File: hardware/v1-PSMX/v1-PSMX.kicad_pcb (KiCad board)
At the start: 2 copper layers, 3 parts, among them IC1 MAX98357AETE+T, U1 ESP32-S3-WROOM-1

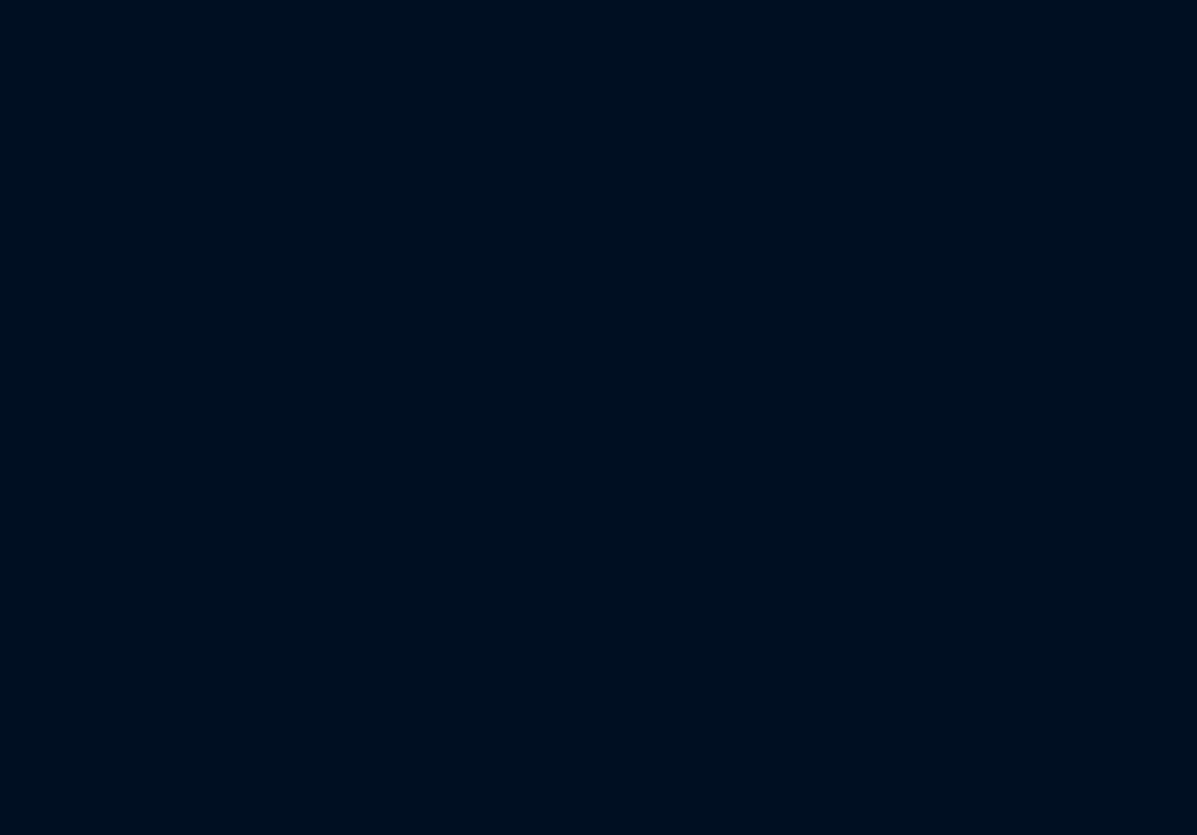
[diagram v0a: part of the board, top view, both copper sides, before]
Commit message: Completed Init work on schematic
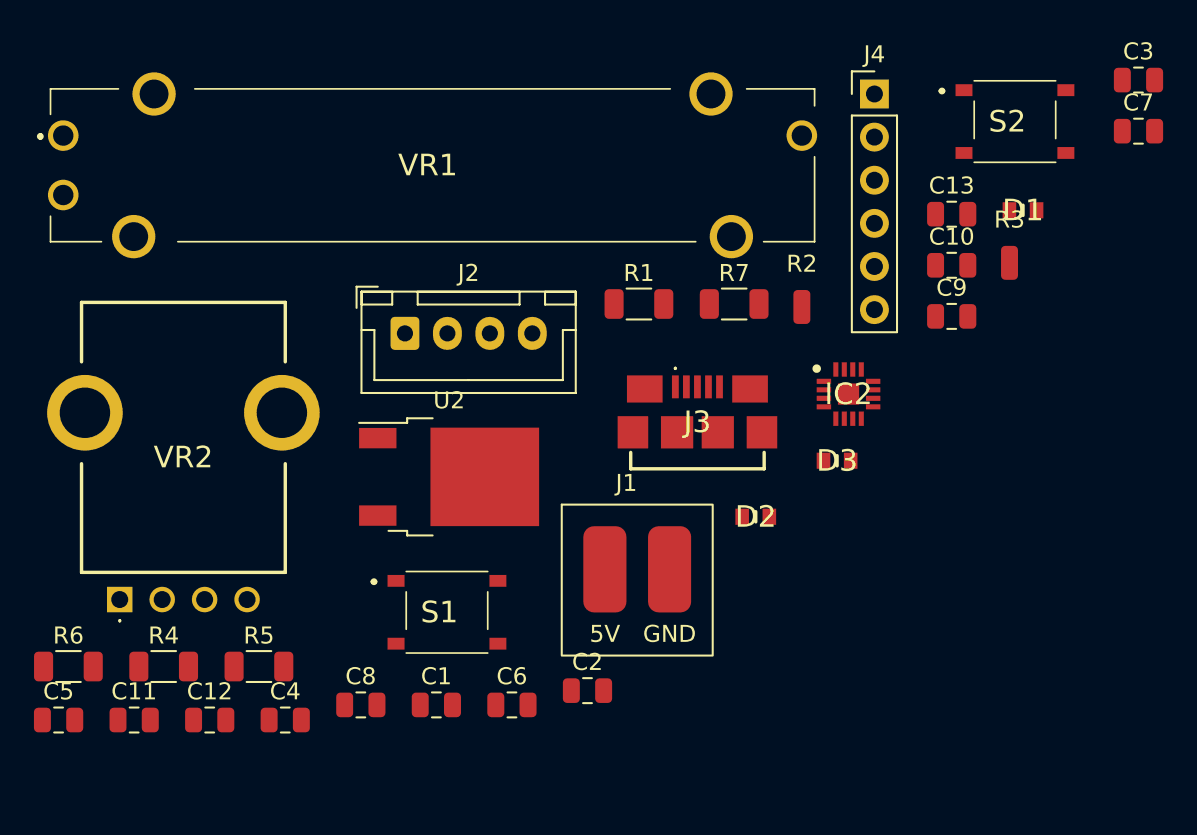
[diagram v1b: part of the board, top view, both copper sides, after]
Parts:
- added C1: 10uF, Capacitor_SMD:C_0805_2012Metric, F.Cu at (126.4, 81.9)
- added C10: 10uF, Capacitor_SMD:C_0805_2012Metric, F.Cu at (156.7, 56.0)
- added C11: 0.1uF, Capacitor_SMD:C_0805_2012Metric, F.Cu at (108.6, 82.8)
- added C12: 0.1uF, Capacitor_SMD:C_0805_2012Metric, F.Cu at (113.0, 82.8)
- added C13: 10uF, Capacitor_SMD:C_0805_2012Metric, F.Cu at (156.7, 53.0)
- added C2: 0.1uF, Capacitor_SMD:C_0805_2012Metric, F.Cu at (135.3, 81.1)
- added C3: 0.1uF, Capacitor_SMD:C_0805_2012Metric, F.Cu at (167.7, 45.1)
- added C4: 10uF, Capacitor_SMD:C_0805_2012Metric, F.Cu at (117.5, 82.8)
- added C5: 10uF, Capacitor_SMD:C_0805_2012Metric, F.Cu at (104.1, 82.8)
- added C6: 10uF, Capacitor_SMD:C_0805_2012Metric, F.Cu at (130.8, 81.9)
- added C7: 0.1uF, Capacitor_SMD:C_0805_2012Metric, F.Cu at (167.7, 48.1)
- added C8: 0.1uF, Capacitor_SMD:C_0805_2012Metric, F.Cu at (121.9, 81.9)
- added C9: 0.1uF, Capacitor_SMD:C_0805_2012Metric, F.Cu at (156.7, 59.0)
- added D1: GG060305100N2P, my-footprints:DIONC1608X70N, F.Cu at (160.9, 52.8)
- added D2: GG060305100N2P, my-footprints:DIONC1608X70N, F.Cu at (145.2, 70.8)
- added D3: GG060305100N2P, my-footprints:DIONC1608X70N, F.Cu at (150.0, 67.5)
- added IC2: MAX98357AETE+T (R), MAX98357AETE+T:QFN50P300X300X80-17N, F.Cu at (150.6, 63.6)
- added J1: +5v_POWER, my-footprints:CUSTOM_5V_SOLDER_PADS, F.Cu at (137.6, 73.9)
- added J2: Conn_01x04, Connector_JST:JST_XH_B4B-XH-A_1x04_P2.50mm_Vertical, F.Cu at (124.5, 60.0)
- added J3: 10118192-0002LF, my-footprints:101181920002LF, F.Cu at (141.7, 65.5)
- added J4: Serial_Breakout, Connector_PinHeader_2.54mm:PinHeader_1x06_P2.54mm_Vertical, F.Cu at (152.2, 45.9)
- added R1: 270ohm, Resistor_SMD:R_1206_3216Metric, F.Cu at (138.3, 58.3)
- added R2: GAIN SELECT, Connector_Wire:SolderWirePad_1x01_SMD_1x2mm, F.Cu at (147.9, 58.5)
- added R3: GAIN SELECT, Connector_Wire:SolderWirePad_1x01_SMD_1x2mm, F.Cu at (160.1, 55.9)
- added R4: 270ohm, Resistor_SMD:R_1206_3216Metric, F.Cu at (110.3, 79.7)
- added R5: 270ohm, Resistor_SMD:R_1206_3216Metric, F.Cu at (115.9, 79.7)
- added R6: 10k_ohm, Resistor_SMD:R_1206_3216Metric, F.Cu at (104.7, 79.7)
- added R7: 220k_ohm, Resistor_SMD:R_1206_3216Metric, F.Cu at (143.9, 58.3)
- added S1: PTS526_SM08_SMTR2_LFS, my-footprints:PTS526SM08SMTR2LFS, F.Cu at (127.0, 76.5)
- added S2: PTS526_SM08_SMTR2_LFS, my-footprints:PTS526SM08SMTR2LFS, F.Cu at (160.4, 47.6)
- added U2: AZ1084-3.3, Package_TO_SOT_SMD:TO-252-2, F.Cu at (127.1, 68.5)
- added VR1: PTA3043-2015DPB104, my-footprints:PTA30432015DPB104, F.Cu at (104.4, 48.4)
- added VR2: P110KH1-0F15BR10K, my-footprints:P110KH10F15BR10K, F.Cu at (107.7, 75.7)
- IC1: value MAX98357AETE+T -> MAX98357AETE+T (L)
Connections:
- IC1 pad 1: unconnected-(IC1-Pad1) -> /DIN_GPIO12
- IC1 pad 10: unconnected-(IC1-Pad10) -> /LEFT_SPK+
- IC1 pad 11: unconnected-(IC1-Pad11) -> GND
- IC1 pad 14: unconnected-(IC1-Pad14) -> /LRCLK_GPIO14
- IC1 pad 15: unconnected-(IC1-Pad15) -> GND
- IC1 pad 16: unconnected-(IC1-Pad16) -> /BCLK_GPIO13
- IC1 pad 17: unconnected-(IC1-Pad17) -> GND
- IC1 pad 2: unconnected-(IC1-Pad2) -> /GAIN_SLOT
- IC1 pad 3: unconnected-(IC1-Pad3) -> GND
- IC1 pad 4: unconnected-(IC1-Pad4) -> /SD_MODE_GPIO11
- IC1 pad 7: unconnected-(IC1-Pad7) -> +5V
- IC1 pad 8: unconnected-(IC1-Pad8) -> +5V
- IC1 pad 9: unconnected-(IC1-Pad9) -> /LEFT_SPK-
- LED1 pad 1: unconnected-(LED1-Pad1) -> +3.3V
- LED1 pad 2: unconnected-(LED1-Pad2) -> Net-(LED1-Pad2)
- LED1 pad 3: unconnected-(LED1-Pad3) -> Net-(LED1-Pad3)
- LED1 pad 4: unconnected-(LED1-Pad4) -> Net-(LED1-Pad4)
- U1 pad 1: Net-(U1-Pad1) -> GND
- U1 pad 13: unconnected-(U1-Pad13) -> /GPIO19_USB_D-
- U1 pad 14: unconnected-(U1-Pad14) -> /GPIO20_USB_D+
- U1 pad 17: unconnected-(U1-Pad17) -> /S_POT_GPIO9
- U1 pad 18: unconnected-(U1-Pad18) -> /V_POT_GPIO10
- U1 pad 19: unconnected-(U1-Pad19) -> /SD_MODE_GPIO11
- U1 pad 2: unconnected-(U1-Pad2) -> +3.3V
- U1 pad 20: unconnected-(U1-Pad20) -> /DIN_GPIO12
- U1 pad 21: unconnected-(U1-Pad21) -> /BCLK_GPIO13
- U1 pad 22: unconnected-(U1-Pad22) -> /LRCLK_GPIO14
- U1 pad 27: unconnected-(U1-Pad27) -> /RST_TO_PRGM
- U1 pad 3: unconnected-(U1-Pad3) -> /RESET
- U1 pad 36: unconnected-(U1-Pad36) -> /U0RXD_TX
- U1 pad 37: unconnected-(U1-Pad37) -> /U0TXD_RX
- U1 pad 4: unconnected-(U1-Pad4) -> /LED_RED_GPIO4
- U1 pad 40: Net-(U1-Pad1) -> GND
- U1 pad 41: Net-(U1-Pad1) -> GND
- U1 pad 5: unconnected-(U1-Pad5) -> /LED_GREEN_GPIO5
- U1 pad 6: unconnected-(U1-Pad6) -> /LED_BLUE_GPIO6

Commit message: init work on pcb
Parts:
- R2: value GAIN SELECT -> GAIN SELECT HIGH; footprint Connector_Wire:SolderWirePad_1x01_SMD_1x2mm -> Resistor_SMD:R_1206_3216Metric
- R3: value GAIN SELECT -> GAIN SELECT LOW; footprint Connector_Wire:SolderWirePad_1x01_SMD_1x2mm -> Resistor_SMD:R_1206_3216Metric
- U1: footprint Espressif:ESP32-S3-WROOM-1 -> Espressif:ESP32-S3-WROOM-1U
- moved VR2 80.0 mm to (177.1, 115.6)
- moved VR1 77.7 mm to (103.4, 126.1), turned to 90 degrees
- moved C7 76.9 mm to (138.7, 119.3), turned to 90 degrees
- moved R3 75.4 mm to (131.1, 125.4), turned to 90 degrees
- moved R1 74.2 mm to (167.6, 126.5)
- moved R4 71.5 mm to (167.6, 122.4)
- moved J2 70.4 mm to (152.4, 124.7), turned to 90 degrees
- moved R2 70.1 mm to (127.0, 125.4), turned to 90 degrees
- moved R7 67.7 mm to (135.1, 125.4), turned to 90 degrees
- moved C3 66.7 mm to (118.4, 89.9), turned to 90 degrees
- moved R5 64.6 mm to (167.6, 118.4)
- moved C9 60.0 mm to (129.0, 112.3), turned to -90 degrees
- moved C13 59.8 mm to (156.8, 112.8), turned to 180 degrees
- moved IC2 57.8 mm to (133.6, 118.8)
- moved C12 51.4 mm to (156.8, 109.7), turned to 180 degrees
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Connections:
- C8 pad 1: /V_POT_GPIO10 -> /V_POT_GPIO09
- C9 pad 1: /S_POT_GPIO9 -> /S_POT_GPIO10
- U1 pad 17: /S_POT_GPIO9 -> /V_POT_GPIO09
- U1 pad 18: /V_POT_GPIO10 -> /S_POT_GPIO10
- VR1 pad 2: /V_POT_GPIO10 -> /V_POT_GPIO09
- VR2 pad 2: /S_POT_GPIO9 -> /S_POT_GPIO10
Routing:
- net GND: track 0.00 -> 35.2 mm, vias 0 -> 38
- added copper zone on B.Cu, net GND
- added copper zone on F.Cu, net GND
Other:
- board outline added: 91.4 x 48.8 mm

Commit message: all routed, but needs organized
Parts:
- J4: footprint Connector_PinHeader_2.54mm:PinHeader_1x06_P2.54mm_Vertical -> Connector_PinHeader_2.54mm:PinHeader_2x02_P2.54mm_Vertical
- moved S2 65.5 mm to (115.3, 86.4), turned to -90 degrees
- moved J2 45.3 mm to (130.8, 84.9), turned to 180 degrees
- moved C4 43.8 mm to (139.7, 125.9), turned to -90 degrees
- moved C3 40.6 mm to (137.2, 125.9), turned to -90 degrees
- moved R6 36.8 mm to (140.2, 122.4)
- moved C6 36.2 mm to (116.2, 94.7), turned to 180 degrees
- moved R7 32.7 mm to (120.9, 96.0), turned to -90 degrees
- moved C7 31.5 mm to (116.2, 97.3), turned to 180 degrees
- moved C5 30.6 mm to (113.3, 107.7), turned to 0 degrees
- moved R1 29.8 mm to (140.2, 114.8)
- moved R4 27.9 mm to (140.2, 117.3)
- moved R5 27.5 mm to (140.2, 119.9)
- moved R2 26.0 mm to (133.6, 100.3), turned to -90 degrees
- moved C1 25.4 mm to (125.5, 94.7), turned to 0 degrees
- moved R3 25.1 mm to (130.6, 100.3), turned to -90 degrees
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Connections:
- C8 pad 1: /V_POT_GPIO09 -> /S_POT_GPIO02
- C9 pad 1: /S_POT_GPIO10 -> /V_POT_GPIO09
- J4 pad 3: /RST_TO_PRGM -> /U0RXD_TX
- J4 pad 4: /RESET -> /U0TXD_RX
- U1 pad 18: /S_POT_GPIO10 -> unconnected-(U1-Pad18)
- U1 pad 38: unconnected-(U1-Pad38) -> /S_POT_GPIO02
- VR1 pad 2: /V_POT_GPIO09 -> /S_POT_GPIO02
- VR2 pad 2: /S_POT_GPIO10 -> /V_POT_GPIO09
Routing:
- net +5V: track 0.00 -> 142.1 mm, vias 0 -> 2
- net /RESET: track 0.00 -> 131.8 mm, vias 0 -> 2
- net +3.3V: track 0.00 -> 110.3 mm, vias 0 -> 2
- net /U0TXD_RX: track 0.00 -> 75.1 mm, vias 0 -> 4
- net /U0RXD_TX: track 0.00 -> 71.1 mm, vias 0 -> 4
- net /V_POT_GPIO09: track 0.00 -> 56.9 mm, vias 0 -> 4
- net Net-(LED1-Pad2): track 0.00 -> 48.2 mm
- net Net-(LED1-Pad3): track 0.00 -> 41.8 mm
- net Net-(LED1-Pad4): track 0.00 -> 41.7 mm, vias 0 -> 2
- net /GPIO19_USB_D-: track 0.00 -> 33.3 mm
- net GND: track 35.2 -> 67.6 mm, vias 38 -> 44
- net /GPIO20_USB_D+: track 0.00 -> 31.9 mm
- net /SD_MODE_GPIO11: track 0.00 -> 31.3 mm, vias 0 -> 2
- net /RST_TO_PRGM: track 0.00 -> 28.5 mm
- net /RIGHT_SPK+: track 0.00 -> 25.0 mm, vias 0 -> 2
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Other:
- outline, holes or cut-outs redrawn

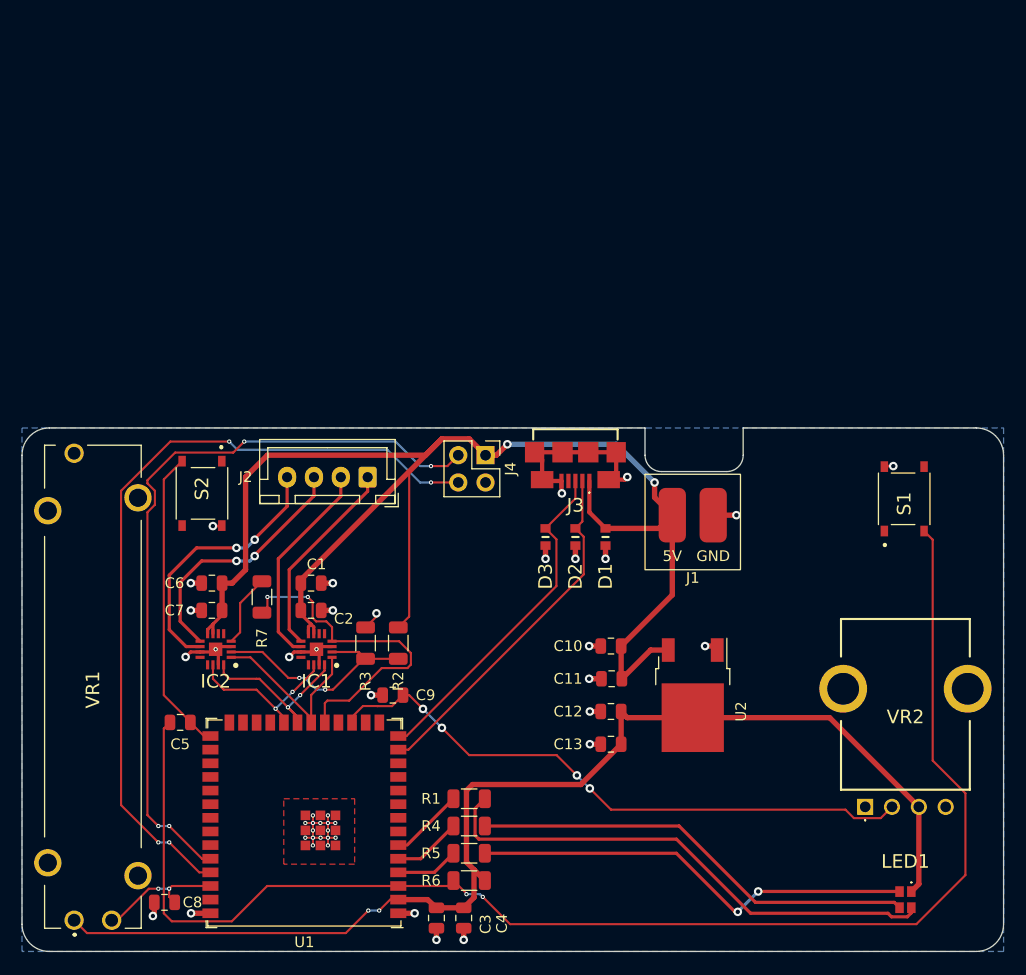
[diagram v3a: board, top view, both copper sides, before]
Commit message: Cleaned up pcb
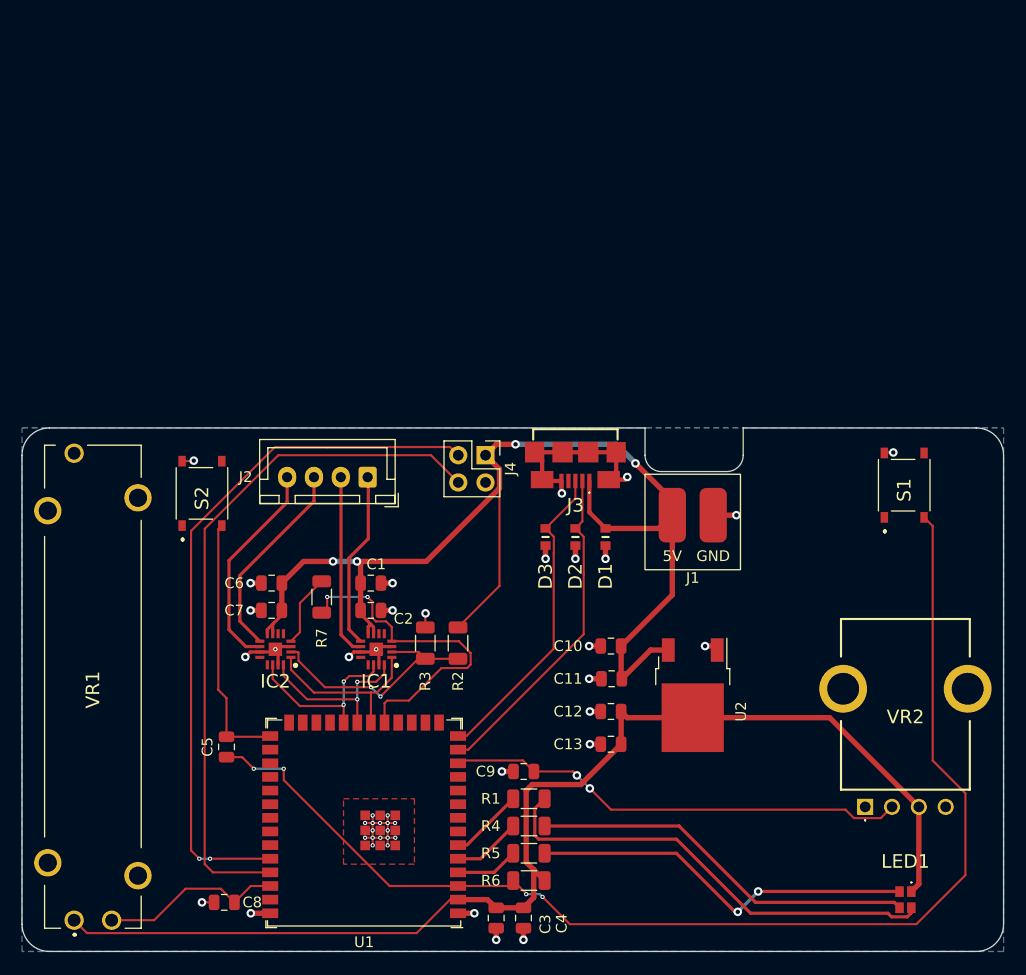
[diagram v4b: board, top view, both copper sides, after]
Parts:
- moved C9 14.1 mm to (145.3, 112.3)
- moved IC1 5.57 mm to (131.6, 100.9)
- moved C1 5.57 mm to (131.0, 94.7)
- moved C2 5.57 mm to (131.0, 97.3)
- moved C3 5.57 mm to (142.7, 125.9)
- moved C4 5.57 mm to (145.3, 125.9)
- moved C6 5.57 mm to (121.8, 94.7)
- moved C7 5.57 mm to (121.8, 97.3)
- moved C8 5.57 mm to (117.4, 124.5)
- moved IC2 5.57 mm to (122.2, 100.9)
- moved R1 5.57 mm to (145.8, 114.8)
- moved R3 5.57 mm to (136.1, 100.3)
- moved R4 5.57 mm to (145.8, 117.3)
- moved R5 5.57 mm to (145.8, 119.9)
- moved R6 5.57 mm to (145.8, 122.4)
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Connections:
- C9 pad 1: /V_POT_GPIO09 -> /V_POT_GPIO08
- U1 pad 12: unconnected-(U1-Pad12) -> /V_POT_GPIO08
- U1 pad 17: /V_POT_GPIO09 -> unconnected-(U1-Pad17)
- VR2 pad 2: /V_POT_GPIO09 -> /V_POT_GPIO08
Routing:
- net /V_POT_GPIO09: track 56.9 -> 0.00 mm, vias 4 -> 0
- net /V_POT_GPIO08: track 0.00 -> 43.2 mm, vias 0 -> 2
- net +5V: track 142.1 -> 114.2 mm, vias 2 -> 4
- net /RESET: track 131.8 -> 113.2 mm, vias 2 -> 4
- net /U0TXD_RX: track 75.1 -> 65.2 mm, vias 4 -> 0
- net Net-(LED1-Pad2): track 48.2 -> 42.6 mm
- net Net-(LED1-Pad4): track 41.7 -> 36.1 mm
- net Net-(LED1-Pad3): track 41.8 -> 36.2 mm
- net /U0RXD_TX: track 71.1 -> 65.9 mm, vias 4 -> 2
- net /S_POT_GPIO02: track 12.0 -> 17.1 mm, vias 2 -> 0
- net /RIGHT_SPK+: track 25.0 -> 20.0 mm, vias 2 -> 0
- net /RIGHT_SPK-: track 23.8 -> 18.9 mm, vias 2 -> 0
- net /RST_TO_PRGM: track 28.5 -> 24.2 mm
- net /LEFT_SPK+: track 19.5 -> 17.0 mm
- net /GPIO20_USB_D+: track 31.9 -> 29.4 mm
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
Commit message: added silk screen labels for resistor and diode size
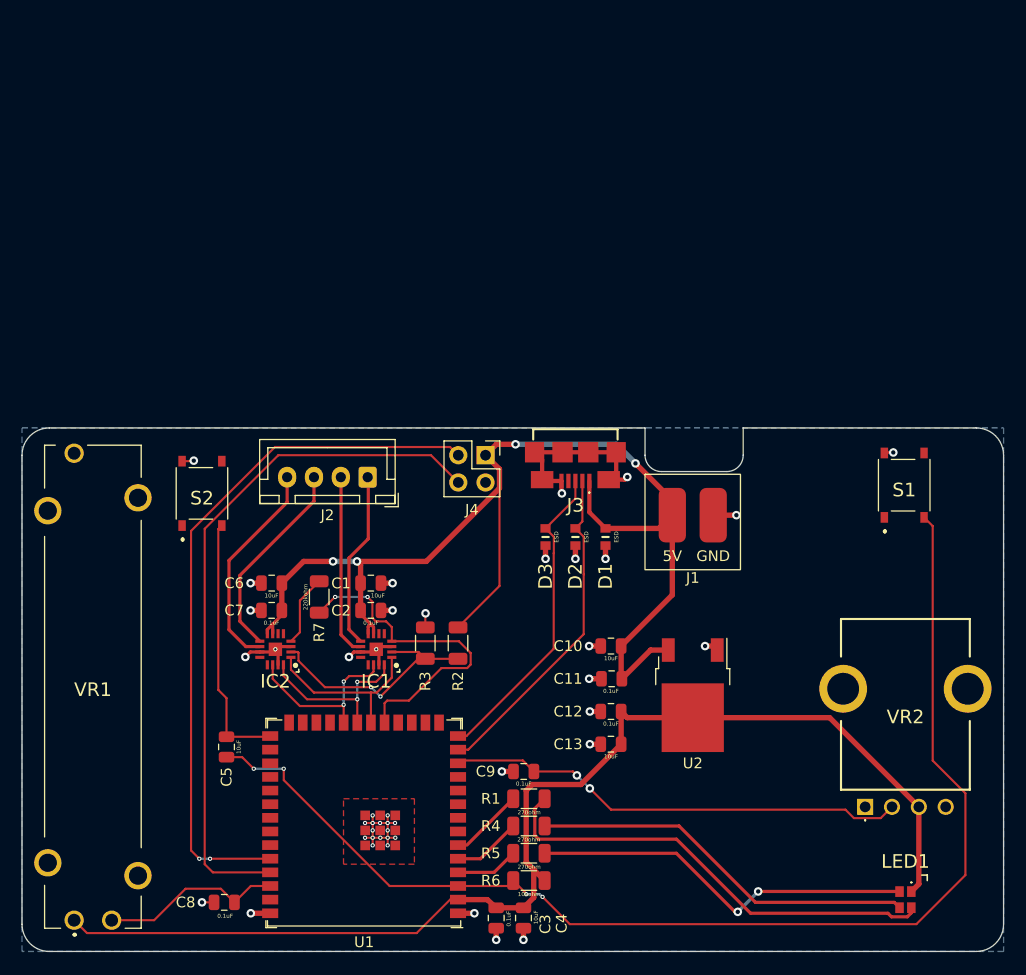
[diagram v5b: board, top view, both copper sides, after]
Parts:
- moved R7 0.23 mm to (126.2, 96.0)
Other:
- board text added: "0.1uF"
- board text added: "10kohm"
- board text added: "10uF"
- board text added: "220kohm"
- board text added: "270ohm"
- board text added: "ESD"

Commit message: added version number
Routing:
- net /U0RXD_TX: track 65.9 -> 66.7 mm
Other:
- board text added: "v1-PSMX.test-1"
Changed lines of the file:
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@@
       (effects (font (size 1 1) (thickness 0.15)))
     )
-    (fp_text user "${REFERENCE}" (at 0 0) (layer "F.Fab")
+    (fp_text user "${REFERENCE}" (at 0 6.472) (layer "F.Fab")
       (effects (font (size 1 1) (thickness 0.15)))
     )
@@
   (gr_text "0.1uF" (at 153.416 107.823) (layer "F.SilkS")
     (effects (font (size 0.381 0.381) (thickness 0.09525)))
+  )
+  (gr_text "v1-PSMX.test-1" (at 180.975 127.889) (layer "F.SilkS")
+    (effects (font (size 1 1) (thickness 0.15)))
   )
   (gr_text "10uF" (at 153.416 101.727) (layer "F.SilkS")
@@
   (segment (start 119.408 100.634) (end 120.706 100.634) (width 0.3) (layer "F.Cu") (net 28))
   (segment (start 117.834 92.605) (end 117.834 99.06) (width 0.3) (layer "F.Cu") (net 28))
+  (segment (start 122.047 81.534) (end 137.922 81.534) (width 0.2) (layer "F.Cu") (net 34))
   (segment (start 115.0705 120.396) (end 114.3 119.6255) (width 0.2) (layer "F.Cu") (net 34))
-  (segment (start 138.43 82.042) (end 139.192 82.804) (width 0.2) (layer "F.Cu") (net 34))
-  (segment (start 122.116314 82.042) (end 138.43 82.042) (width 0.2) (layer "F.Cu") (net 34))
-  (segment (start 114.3 89.858314) (end 122.116314 82.042) (width 0.2) (layer "F.Cu") (net 34))
+  (segment (start 114.3 119.6255) (end 114.3 89.281) (width 0.2) (layer "F.Cu") (net 34))
+  (segment (start 137.922 81.534) (end 139.192 82.804) (width 0.2) (layer "F.Cu") (net 34))
+  (segment (start 114.3 89.281) (end 122.047 81.534) (width 0.2) (layer "F.Cu") (net 34))
   (segment (start 116.0695 120.396) (end 121.67 120.396) (width 0.2) (layer "F.Cu") (net 34))
-  (segment (start 114.3 119.6255) (end 114.3 89.858314) (width 0.2) (layer "F.Cu") (net 34))
   (via (at 116.0695 120.396) (size 0.4) (drill 0.2) (layers "F.Cu" "B.Cu") (net 34))
   (via (at 115.0705 120.396) (size 0.4) (drill 0.2) (layers "F.Cu" "B.Cu") (net 34))
